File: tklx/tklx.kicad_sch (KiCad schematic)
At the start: 10 parts

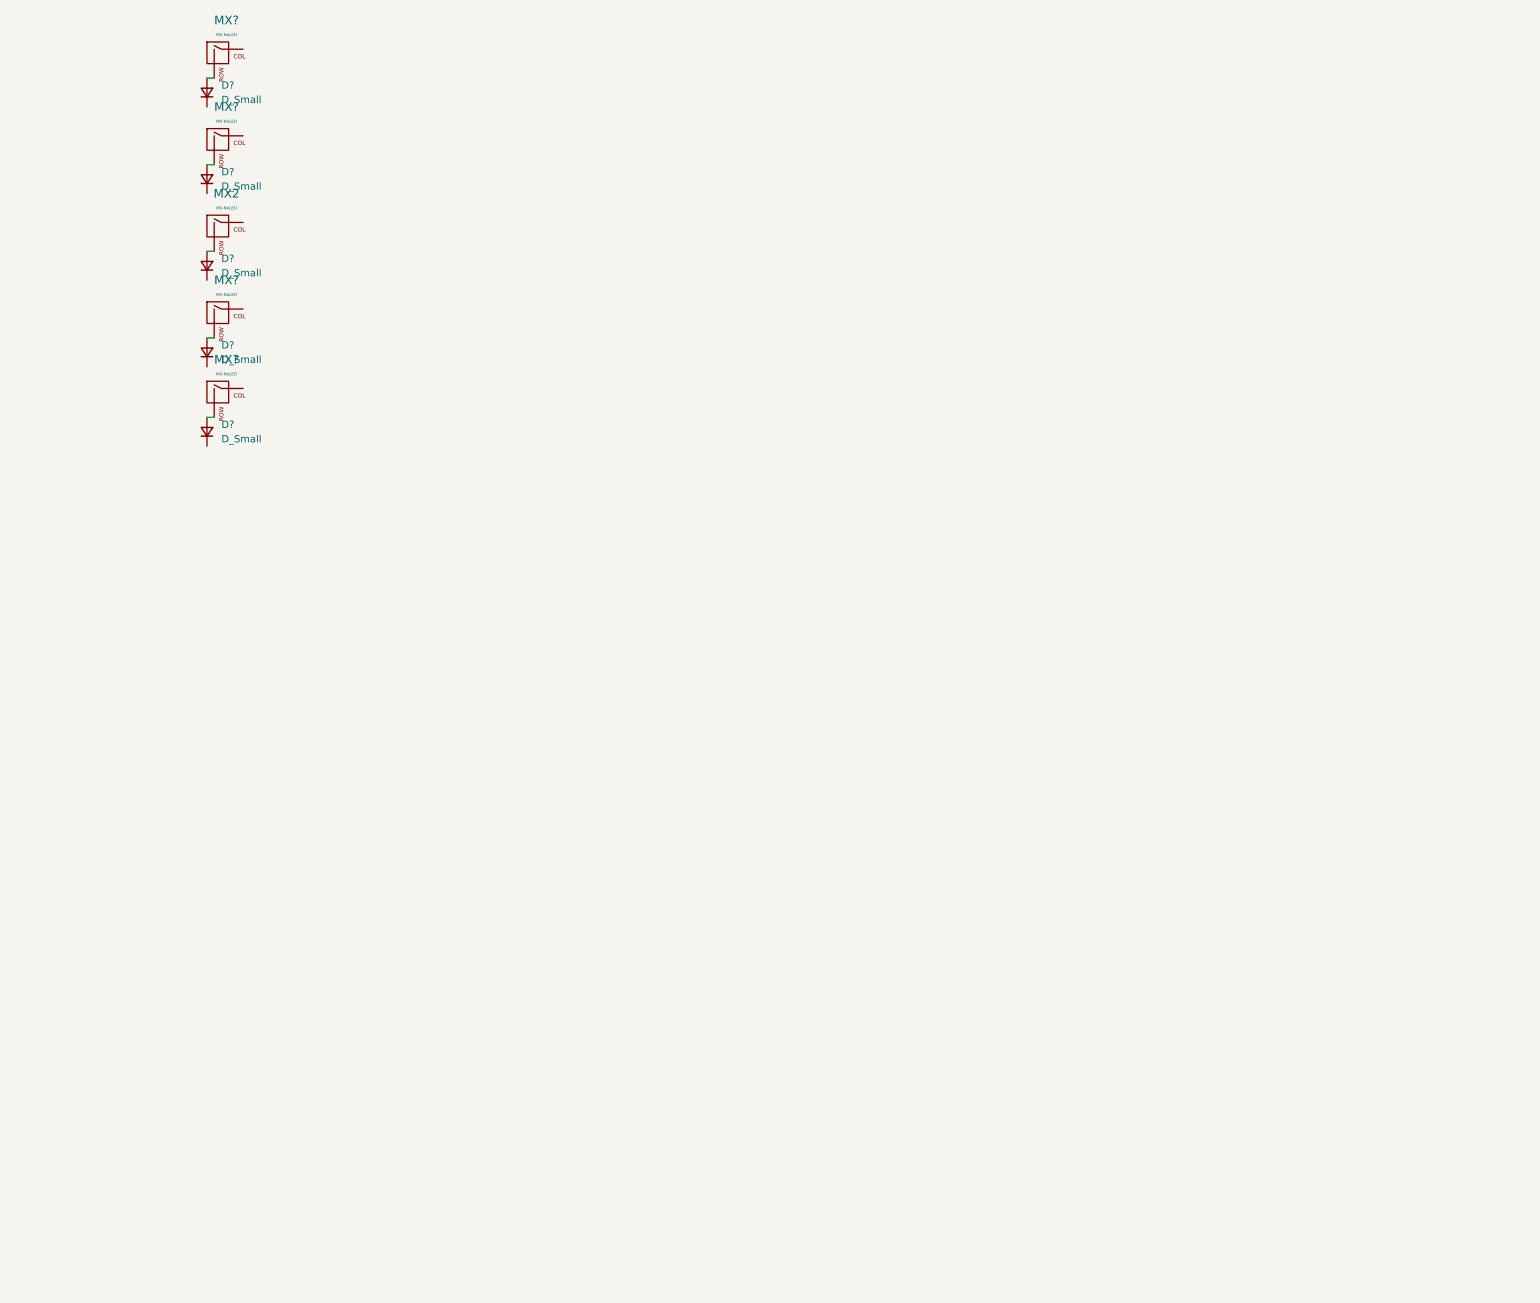
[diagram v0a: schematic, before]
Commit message: finished wiring for switches
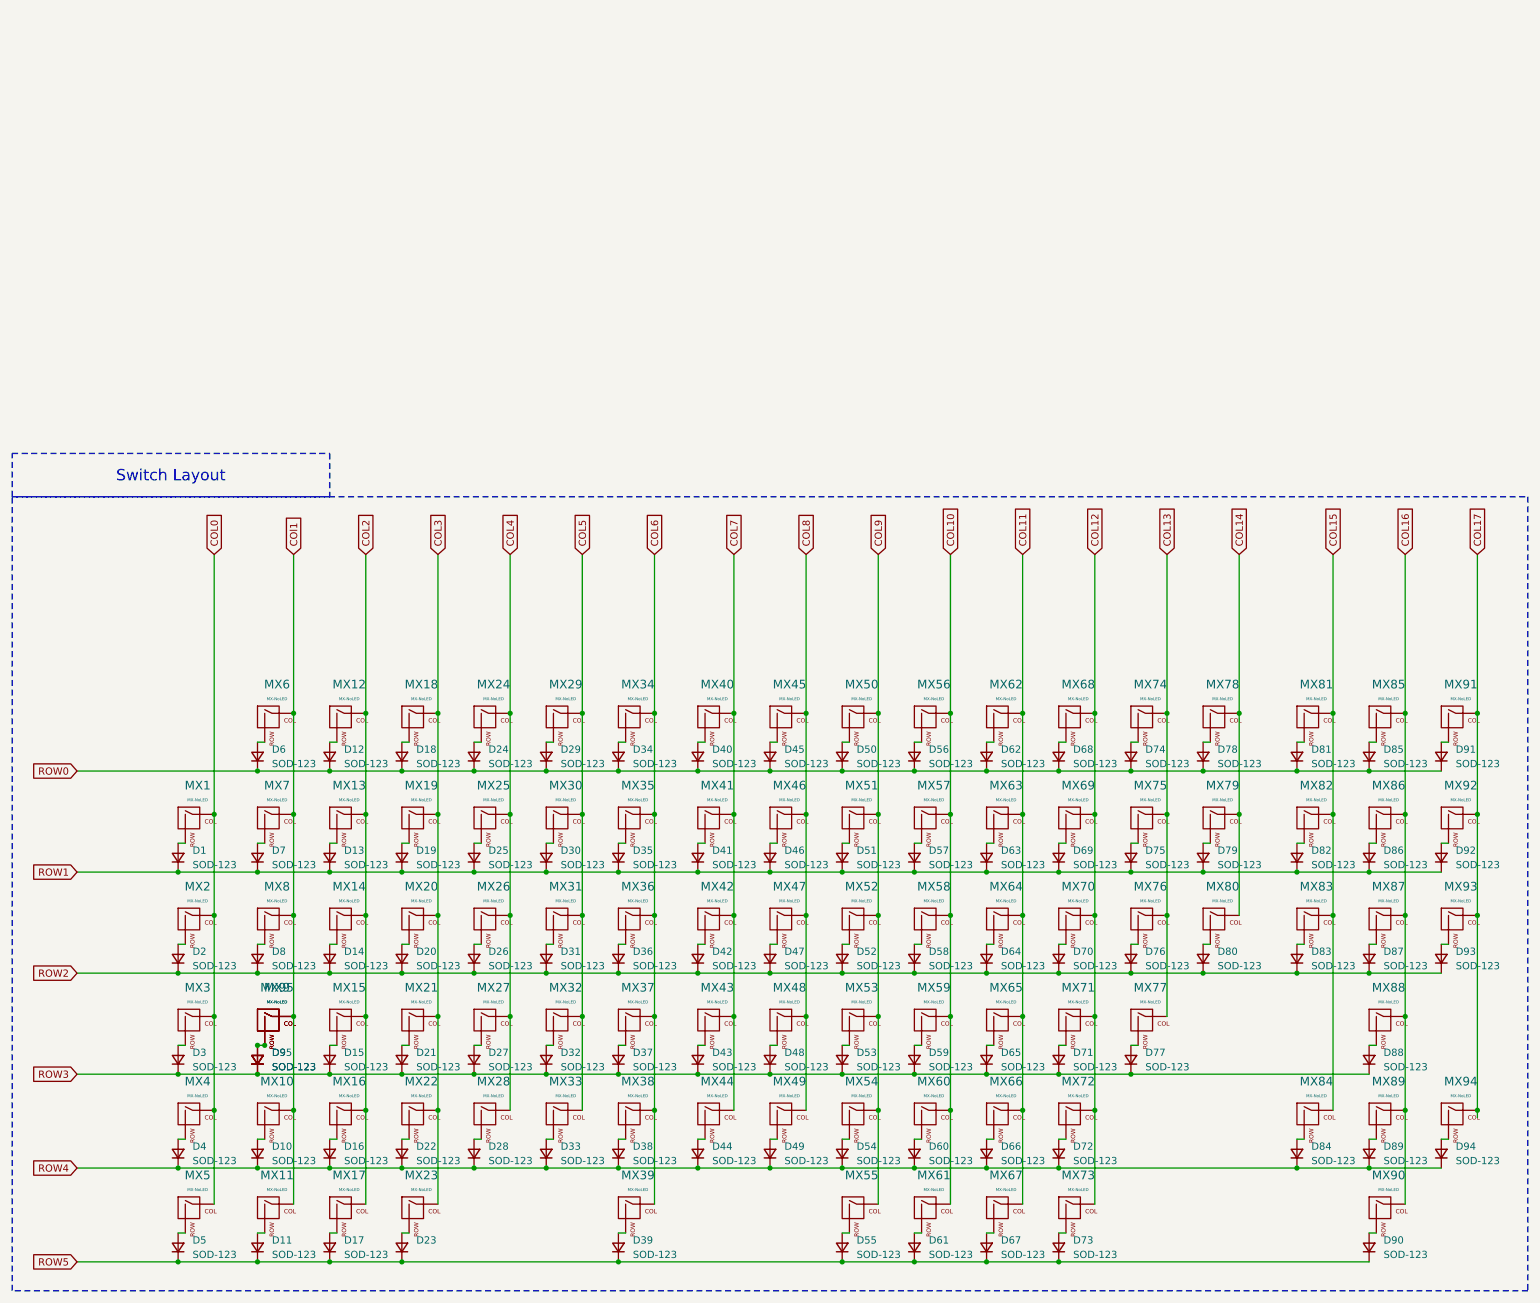
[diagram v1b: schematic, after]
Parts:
- removed D? (x5): D_Small, symbol Device:D_Small
- removed MX? (x4): MX-NoLED, symbol MX_Alps_Hybrid:MX-NoLED
- added D1, D10, D11, D12, D13, D14, D15, D16, D17, D18, D19, D2, D20, D21, D22, D23, D24, D25, D26, D27, D28, D29, D3, D30, D31, D32, D33, D34, D35, D36, D37, D38, D39, D4, D40, D41, D42, D43, D44, D45, D46, D47, D48, D49, D5, D50, D51, D52, D53, D54, D55, D56, D57, D58, D59, D6, D60, D61, D62, D63, D64, D65, D66, D67, D68, D69, D7, D70, D71, D72, D73, D74, D75, D76, D77, D78, D79, D8, D80, D81, D82, D83, D84, D85, D86, D87, D88, D89, D9, D90, D91, D92, D93, D94, D95: SOD-123, Diode_SMD:D_SOD-123, symbol Device:D_Small
- added MX1, MX12, MX13, MX14, MX15, MX16, MX18, MX19, MX20, MX21, MX22, MX24, MX25, MX26, MX27, MX28, MX29, MX3, MX30, MX31, MX32, MX33, MX34, MX35, MX36, MX37, MX38, MX4, MX40, MX41, MX42, MX43, MX44, MX45, MX46, MX47, MX48, MX49, MX5, MX50, MX51, MX52, MX53, MX54, MX56, MX57, MX58, MX59, MX6, MX60, MX62, MX63, MX64, MX65, MX66, MX68, MX69, MX7, MX70, MX71, MX72, MX74, MX75, MX76, MX78, MX81, MX82, MX83, MX84, MX85, MX86, MX87, MX88, MX89, MX90, MX91, MX92, MX93, MX94, MX95: MX-NoLED, MX_Only:MXOnly-1U-NoLED, symbol MX_Alps_Hybrid:MX-NoLED
- added MX10, MX80: MX-NoLED, MX_Only:MXOnly-2.25U-NoLED, symbol MX_Alps_Hybrid:MX-NoLED
- added MX11, MX17, MX23, MX55, MX61, MX67, MX73: MX-NoLED, MX_Only:MXOnly-1.25U-NoLED, symbol MX_Alps_Hybrid:MX-NoLED
- added MX39: MX-NoLED, MX_Only:MXOnly-6.25U-NoLED, symbol MX_Alps_Hybrid:MX-NoLED
- added MX77: MX-NoLED, MX_Only:MXOnly-2.75U-NoLED, symbol MX_Alps_Hybrid:MX-NoLED
- added MX79, MX8: MX-NoLED, MX_Only:MXOnly-1.5U-NoLED, symbol MX_Alps_Hybrid:MX-NoLED
- added MX9: MX-NoLED, MX_Only:MXOnly-1.75U-NoLED, symbol MX_Alps_Hybrid:MX-NoLED
- MX2: footprint (none) -> MX_Only:MXOnly-1U-NoLED
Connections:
- net COL0: now reaches MX2.1 (COL)
- net COL0: now also MX1.1 (COL), MX3.1 (COL), MX4.1 (COL), MX5.1 (COL)
- net at MX2.2 (ROW): now also D2.2 (A)
- new net: D30.2 (A), MX30.2 (ROW)
- new net: D73.2 (A), MX73.2 (ROW)
- new net: D49.2 (A), MX49.2 (ROW)
- new net: D61.2 (A), MX61.2 (ROW)
- new net: D16.2 (A), MX16.2 (ROW)
- new net: D31.2 (A), MX31.2 (ROW)
- new net: D35.2 (A), MX35.2 (ROW)
- new net: D10.2 (A), MX10.2 (ROW)
- new net: D20.2 (A), MX20.2 (ROW)
- new net: D47.2 (A), MX47.2 (ROW)
- new net: D91.2 (A), MX91.2 (ROW)
- new net: D32.2 (A), MX32.2 (ROW)
- new net: D7.2 (A), MX7.2 (ROW)
- new net: D17.2 (A), MX17.2 (ROW)
- new net: D83.2 (A), MX83.2 (ROW)
- new net: D72.2 (A), MX72.2 (ROW)
- new net: D18.2 (A), MX18.2 (ROW)
- new net: D42.2 (A), MX42.2 (ROW)
- new net: D80.2 (A), MX80.2 (ROW)
- new net: D29.2 (A), MX29.2 (ROW)
- new net: D63.2 (A), MX63.2 (ROW)
- new net: D26.2 (A), MX26.2 (ROW)
- new net: D23.2 (A), MX23.2 (ROW)
- new net: D4.2 (A), MX4.2 (ROW)
- new net: D8.2 (A), MX8.2 (ROW)
- new net: D78.2 (A), MX78.2 (ROW)
- new net: D9.2 (A), D95.2 (A), MX9.2 (ROW), MX95.2 (ROW)
- new net: D94.2 (A), MX94.2 (ROW)
- new net: D11.2 (A), MX11.2 (ROW)
- new net: D15.2 (A), MX15.2 (ROW)
- new net: D70.2 (A), MX70.2 (ROW)
- new net: D77.2 (A), MX77.2 (ROW)
- new net: D68.2 (A), MX68.2 (ROW)
- new net: D19.2 (A), MX19.2 (ROW)
- new net: D54.2 (A), MX54.2 (ROW)
- new net: D79.2 (A), MX79.2 (ROW)
- new net: D41.2 (A), MX41.2 (ROW)
- new net: D1.2 (A), MX1.2 (ROW)
- new net: D46.2 (A), MX46.2 (ROW)
- new net: D89.2 (A), MX89.2 (ROW)
- new net: D51.2 (A), MX51.2 (ROW)
- new net: D6.2 (A), MX6.2 (ROW)
- new net: D5.2 (A), MX5.2 (ROW)
- new net: D53.2 (A), MX53.2 (ROW)
- new net: D75.2 (A), MX75.2 (ROW)
- new net: D48.2 (A), MX48.2 (ROW)
- new net: D55.2 (A), MX55.2 (ROW)
- new net: D88.2 (A), MX88.2 (ROW)
- new net: D14.2 (A), MX14.2 (ROW)
- new net: D74.2 (A), MX74.2 (ROW)
- new net: D3.2 (A), MX3.2 (ROW)
- new net: D12.2 (A), MX12.2 (ROW)
- new net: D64.2 (A), MX64.2 (ROW)
- new net: D28.2 (A), MX28.2 (ROW)
- new net: D87.2 (A), MX87.2 (ROW)
- new net: D37.2 (A), MX37.2 (ROW)
- new net: D27.2 (A), MX27.2 (ROW)
- new net: D66.2 (A), MX66.2 (ROW)
- new net: D36.2 (A), MX36.2 (ROW)
- new net: D84.2 (A), MX84.2 (ROW)
- new net: D76.2 (A), MX76.2 (ROW)
- new net: D58.2 (A), MX58.2 (ROW)
- new net: D52.2 (A), MX52.2 (ROW)
- new net: D22.2 (A), MX22.2 (ROW)
- new net: D45.2 (A), MX45.2 (ROW)
- new net: D59.2 (A), MX59.2 (ROW)
- new net: D50.2 (A), MX50.2 (ROW)
- new net: D44.2 (A), MX44.2 (ROW)
- new net: D81.2 (A), MX81.2 (ROW)
- new net: D57.2 (A), MX57.2 (ROW)
- new net: D40.2 (A), MX40.2 (ROW)
- new net: D13.2 (A), MX13.2 (ROW)
- new net: D24.2 (A), MX24.2 (ROW)
- new net: D90.2 (A), MX90.2 (ROW)
- new net: D86.2 (A), MX86.2 (ROW)
- new net: D39.2 (A), MX39.2 (ROW)
- new net: D43.2 (A), MX43.2 (ROW)
- new net: D92.2 (A), MX92.2 (ROW)
- new net: D85.2 (A), MX85.2 (ROW)
- new net: D93.2 (A), MX93.2 (ROW)
- new net: D56.2 (A), MX56.2 (ROW)
- new net: D21.2 (A), MX21.2 (ROW)
- new net: D62.2 (A), MX62.2 (ROW)
- new net: D60.2 (A), MX60.2 (ROW)
- new net: D33.2 (A), MX33.2 (ROW)
- new net: D82.2 (A), MX82.2 (ROW)
- new net: D67.2 (A), MX67.2 (ROW)
- new net: D38.2 (A), MX38.2 (ROW)
- new net: D65.2 (A), MX65.2 (ROW)
- new net: D69.2 (A), MX69.2 (ROW)
- new net: D25.2 (A), MX25.2 (ROW)
- new net: D34.2 (A), MX34.2 (ROW)
- new net: D71.2 (A), MX71.2 (ROW)
- new net COL10: MX56.1 (COL), MX57.1 (COL), MX58.1 (COL), MX59.1 (COL), MX60.1 (COL), MX61.1 (COL)
- new net COL11: MX62.1 (COL), MX63.1 (COL), MX64.1 (COL), MX65.1 (COL), MX66.1 (COL), MX67.1 (COL)
- new net COL12: MX68.1 (COL), MX69.1 (COL), MX70.1 (COL), MX71.1 (COL), MX72.1 (COL), MX73.1 (COL)
- new net COL13: MX74.1 (COL), MX75.1 (COL), MX76.1 (COL), MX77.1 (COL)
- new net COL14: MX78.1 (COL), MX79.1 (COL), MX80.1 (COL)
- new net COL15: MX81.1 (COL), MX82.1 (COL), MX83.1 (COL), MX84.1 (COL)
- new net COL16: MX85.1 (COL), MX86.1 (COL), MX87.1 (COL), MX88.1 (COL), MX89.1 (COL), MX90.1 (COL)
- new net COL17: MX91.1 (COL), MX92.1 (COL), MX93.1 (COL), MX94.1 (COL)
- new net COL2: MX12.1 (COL), MX13.1 (COL), MX14.1 (COL), MX15.1 (COL), MX16.1 (COL), MX17.1 (COL)
- new net COL3: MX18.1 (COL), MX19.1 (COL), MX20.1 (COL), MX21.1 (COL), MX22.1 (COL), MX23.1 (COL)
- new net COL4: MX24.1 (COL), MX25.1 (COL), MX26.1 (COL), MX27.1 (COL), MX28.1 (COL)
- new net COL5: MX29.1 (COL), MX30.1 (COL), MX31.1 (COL), MX32.1 (COL), MX33.1 (COL)
- new net COL6: MX34.1 (COL), MX35.1 (COL), MX36.1 (COL), MX37.1 (COL), MX38.1 (COL), MX39.1 (COL)
- new net COL7: MX40.1 (COL), MX41.1 (COL), MX42.1 (COL), MX43.1 (COL), MX44.1 (COL)
- new net COL8: MX45.1 (COL), MX46.1 (COL), MX47.1 (COL), MX48.1 (COL), MX49.1 (COL)
- new net COL9: MX50.1 (COL), MX51.1 (COL), MX52.1 (COL), MX53.1 (COL), MX54.1 (COL), MX55.1 (COL)
- new net COl1: MX10.1 (COL), MX11.1 (COL), MX6.1 (COL), MX7.1 (COL), MX8.1 (COL), MX9.1 (COL), MX95.1 (COL)
- new net ROW0: D12.1 (K), D18.1 (K), D24.1 (K), D29.1 (K), D34.1 (K), D40.1 (K), D45.1 (K), D50.1 (K), D56.1 (K), D6.1 (K), D62.1 (K), D68.1 (K), D74.1 (K), D78.1 (K), D81.1 (K), D85.1 (K), D91.1 (K)
- new net ROW1: D1.1 (K), D13.1 (K), D19.1 (K), D25.1 (K), D30.1 (K), D35.1 (K), D41.1 (K), D46.1 (K), D51.1 (K), D57.1 (K), D63.1 (K), D69.1 (K), D7.1 (K), D75.1 (K), D79.1 (K), D82.1 (K), D86.1 (K), D92.1 (K)
- new net ROW2: D14.1 (K), D2.1 (K), D20.1 (K), D26.1 (K), D31.1 (K), D36.1 (K), D42.1 (K), D47.1 (K), D52.1 (K), D58.1 (K), D64.1 (K), D70.1 (K), D76.1 (K), D8.1 (K), D80.1 (K), D83.1 (K), D87.1 (K), D93.1 (K)
- new net ROW3: D15.1 (K), D21.1 (K), D27.1 (K), D3.1 (K), D32.1 (K), D37.1 (K), D43.1 (K), D48.1 (K), D53.1 (K), D59.1 (K), D65.1 (K), D71.1 (K), D77.1 (K), D88.1 (K), D9.1 (K), D95.1 (K)
- new net ROW4: D10.1 (K), D16.1 (K), D22.1 (K), D28.1 (K), D33.1 (K), D38.1 (K), D4.1 (K), D44.1 (K), D49.1 (K), D54.1 (K), D60.1 (K), D66.1 (K), D72.1 (K), D84.1 (K), D89.1 (K), D94.1 (K)
- new net ROW5: D11.1 (K), D17.1 (K), D23.1 (K), D39.1 (K), D5.1 (K), D55.1 (K), D61.1 (K), D67.1 (K), D73.1 (K), D90.1 (K)
